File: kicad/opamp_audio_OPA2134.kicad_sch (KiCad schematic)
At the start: 24 parts, among them J1 AudioJack3, J2 Conn_Coaxial_x2, U1 OPA2134, U2 OPA2134

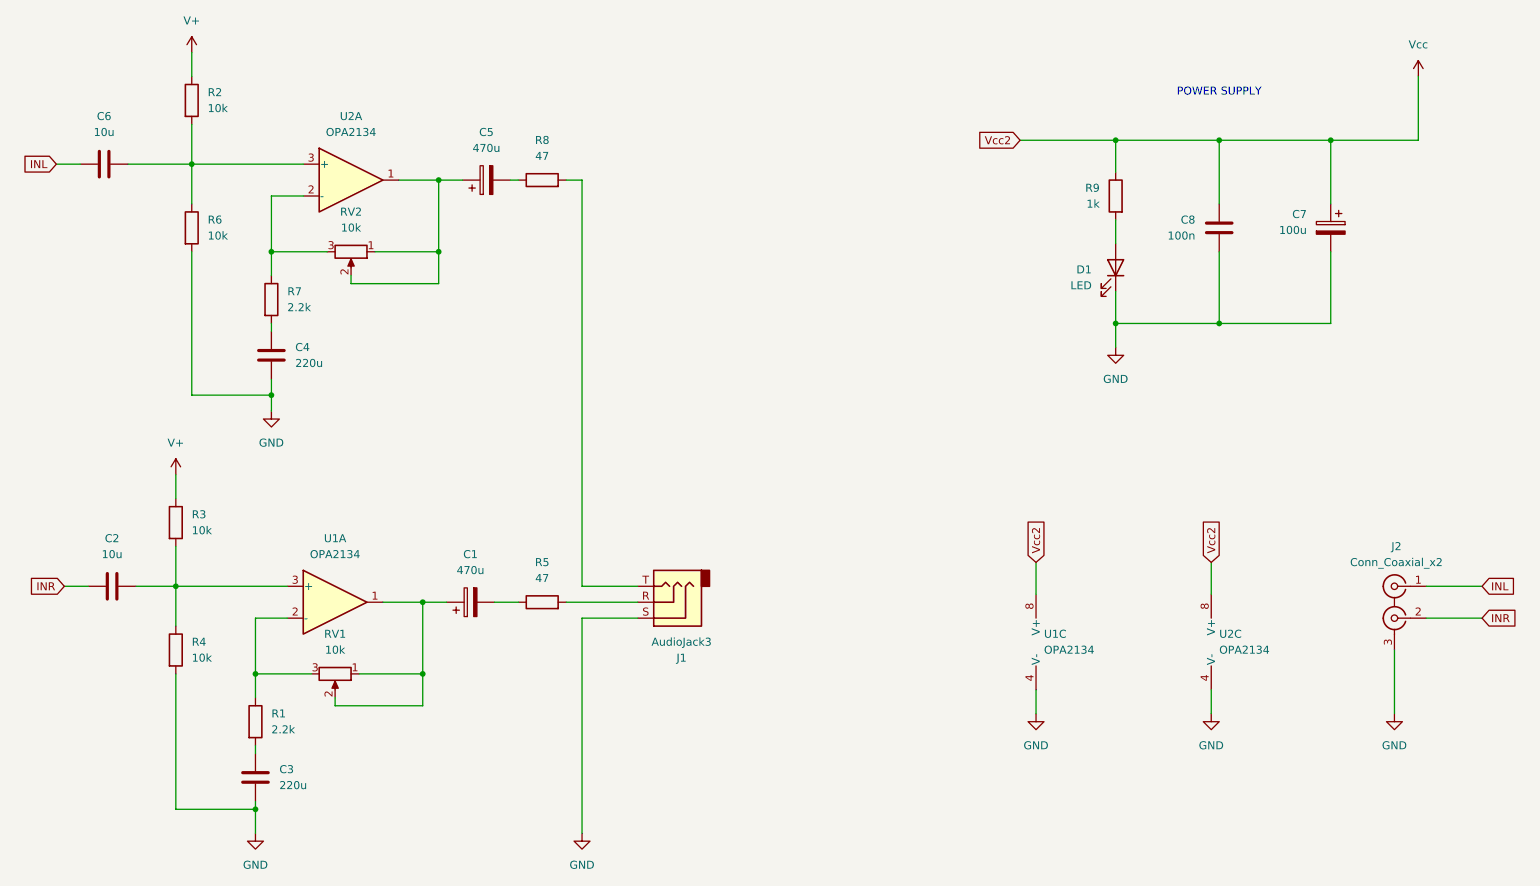
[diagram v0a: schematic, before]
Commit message: changed opamp to TPA6120
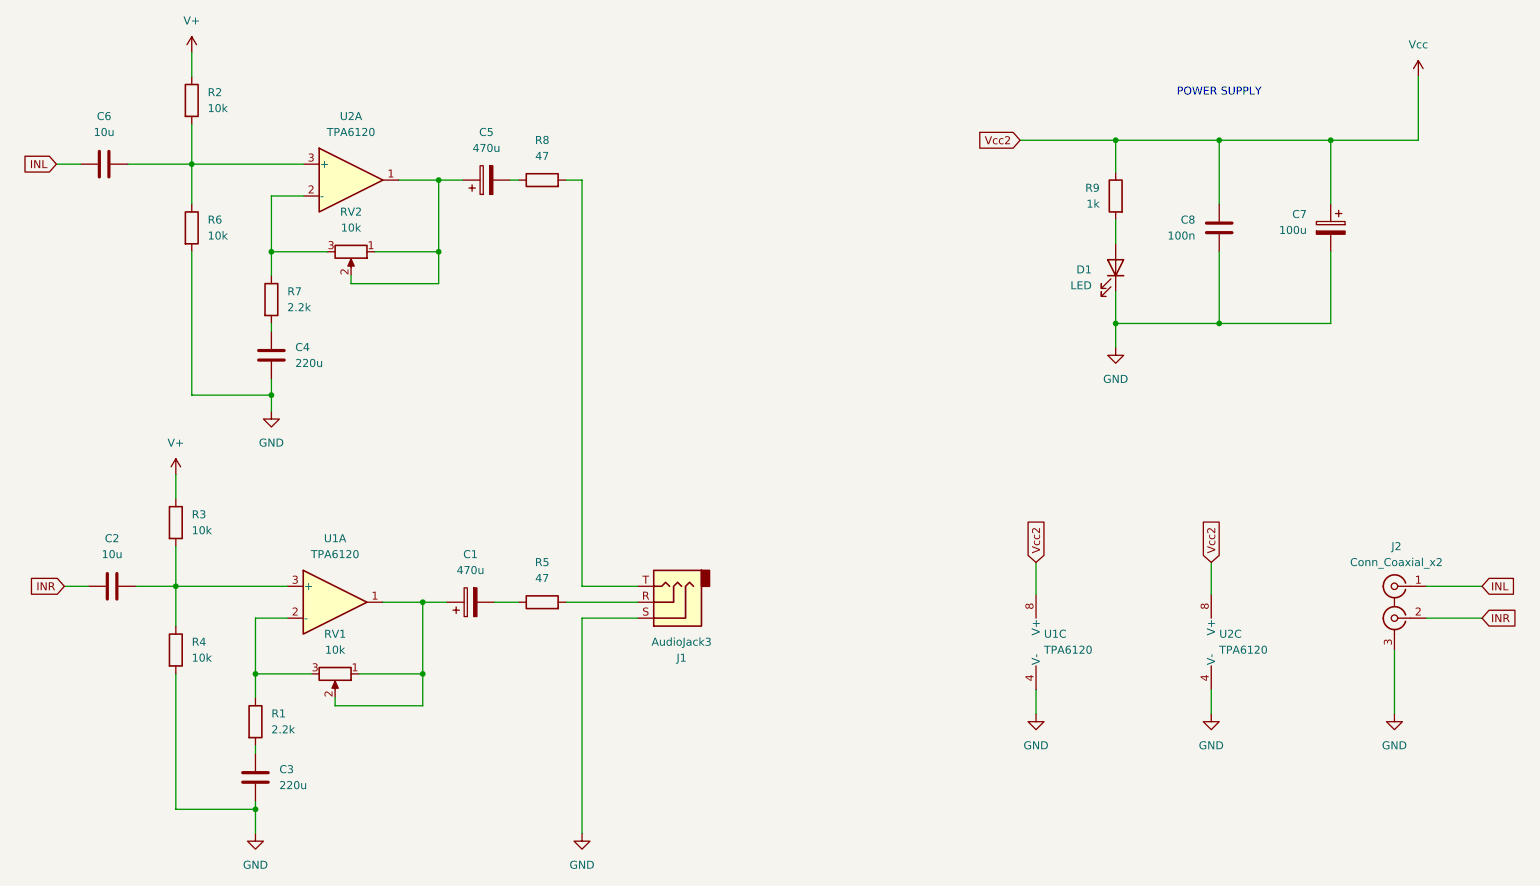
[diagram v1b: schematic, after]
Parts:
- U1, U2: value OPA2134 -> TPA6120
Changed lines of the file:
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@@
 			)
 		)
-		(property "Value" "OPA2134"
+		(property "Value" "TPA6120"
 			(at 88.9 45.72 0)
 			(effects
@@
 			)
 		)
-		(property "Value" "OPA2134"
+		(property "Value" "TPA6120"
 			(at 86.36 113.03 0)
 			(effects
@@
 			)
 		)
-		(property "Value" "OPA2134"
+		(property "Value" "TPA6120"
 			(at 227.33 128.2699 0)
 			(effects
@@
 			)
 		)
-		(property "Value" "OPA2134"
+		(property "Value" "TPA6120"
 			(at 199.39 128.2699 0)
 			(effects
